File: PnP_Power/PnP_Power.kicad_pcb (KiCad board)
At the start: 2 copper layers, 25 parts, among them J1 S2B-PH-K-SLFSN, J2 S4B-PH-K-SLFSN, J3 S4B-PH-K-SLFSN, J4 S4B-PH-K-SLFSN, J5 S4B-PH-K-SLFSN, J6 S4B-PH-K-SLFSN, J7 S4B-PH-K-SLFSN

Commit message: Schematic and Layout Changes
updated schematic logic
added limit switches
added 12V to 5V dc converter
added power jack
added jumpers
added inverter for DIRSW

Started layout placed and organized everything nice. Should need to be adjusted some and then routed.
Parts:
- removed J2, J3, J4, J5, J6, J7: S4B-PH-K-SLFSN, PnP_Footprints:CONN_S4B-PH-K-S_JST
- removed R1: 1.5k, Resistor_SMD:R_0603_1608Metric_Pad0.98x0.95mm_HandSolder
- added C7: 22uF, Capacitor_SMD:C_0603_1608Metric_Pad1.08x0.95mm_HandSolder, F.Cu at (205.0, 145.8)
- added C8: 22uF, Capacitor_SMD:C_0603_1608Metric_Pad1.08x0.95mm_HandSolder, F.Cu at (200.5, 145.8)
- added C9: 0.1uF, Capacitor_SMD:C_0603_1608Metric_Pad1.08x0.95mm_HandSolder, F.Cu at (155.4, 75.2)
- added Conn1: Molex_SL_02, MRDT_Connectors:MOLEX_SL_02_Horizontal, F.Cu at (115.7, 143.3)
- added Conn10: Molex_SL_02, MRDT_Connectors:MOLEX_SL_02_Horizontal, F.Cu at (206.0, 153.5)
- added Conn11: Molex_SL_02, MRDT_Connectors:MOLEX_SL_02_Horizontal, F.Cu at (195.2, 153.5)
- added Conn12: Molex_SL_02, MRDT_Connectors:MOLEX_SL_02_Horizontal, F.Cu at (185.2, 153.5)
- added Conn13: Molex_SL_02, MRDT_Connectors:MOLEX_SL_02_Horizontal, F.Cu at (175.2, 153.5)
- added Conn14: Molex_SL_02, MRDT_Connectors:MOLEX_SL_02_Horizontal, F.Cu at (165.1, 153.5)
- added Conn15: Molex_SL_02, MRDT_Connectors:MOLEX_SL_02_Horizontal, F.Cu at (155.1, 153.5)
- added Conn2: Molex_SL_04, MRDT_Connectors:MOLEX_SL_04_Horizontal, F.Cu at (116.8, 66.0)
- added Conn3: Molex_SL_04, MRDT_Connectors:MOLEX_SL_04_Horizontal, F.Cu at (116.8, 119.1)
- added Conn4: Molex_SL_04, MRDT_Connectors:MOLEX_SL_04_Horizontal, F.Cu at (214.8, 121.4)
- added Conn5: Molex_SL_04, MRDT_Connectors:MOLEX_SL_04_Horizontal, F.Cu at (117.2, 92.2)
- added Conn6: Molex_SL_04, MRDT_Connectors:MOLEX_SL_04_Horizontal, F.Cu at (214.5, 95.0)
- added Conn7: Molex_SL_04, MRDT_Connectors:MOLEX_SL_04_Horizontal, F.Cu at (214.5, 68.3)
- added Conn8: Molex_SL_03, MRDT_Connectors:MOLEX_SL_03_Horizontal, F.Cu at (145.0, 153.5)
- added Conn9: Molex_SL_03, MRDT_Connectors:MOLEX_SL_03_Horizontal, F.Cu at (132.5, 153.5)
- added JP1: Jumper_2_Bridged, Connector_PinHeader_2.54mm:PinHeader_1x02_P2.54mm_Vertical, F.Cu at (131.8, 68.6)
- added JP10: Jumper_2_Bridged, Connector_PinHeader_2.54mm:PinHeader_1x02_P2.54mm_Vertical, F.Cu at (199.9, 66.0)
- added JP11: Jumper_2_Bridged, Connector_PinHeader_2.54mm:PinHeader_1x02_P2.54mm_Vertical, F.Cu at (199.9, 63.5)
- added JP12: Jumper_2_Bridged, Connector_PinHeader_2.54mm:PinHeader_1x02_P2.54mm_Vertical, F.Cu at (199.9, 61.0)
- added JP13: Jumper_2_Bridged, Connector_PinHeader_2.54mm:PinHeader_1x02_P2.54mm_Vertical, F.Cu at (199.6, 92.2)
- added JP14: Jumper_2_Bridged, Connector_PinHeader_2.54mm:PinHeader_1x02_P2.54mm_Vertical, F.Cu at (199.6, 89.6)
- added JP15: Jumper_2_Bridged, Connector_PinHeader_2.54mm:PinHeader_1x02_P2.54mm_Vertical, F.Cu at (199.6, 87.1)
- added JP16: Jumper_2_Bridged, Connector_PinHeader_2.54mm:PinHeader_1x02_P2.54mm_Vertical, F.Cu at (131.8, 95.0)
- added JP17: Jumper_2_Bridged, Connector_PinHeader_2.54mm:PinHeader_1x02_P2.54mm_Vertical, F.Cu at (131.8, 97.5)
- added JP18: Jumper_2_Bridged, Connector_PinHeader_2.54mm:PinHeader_1x02_P2.54mm_Vertical, F.Cu at (131.8, 100.1)
- added JP2: Jumper_2_Bridged, Connector_PinHeader_2.54mm:PinHeader_1x02_P2.54mm_Vertical, F.Cu at (131.8, 71.1)
- added JP3: Jumper_2_Bridged, Connector_PinHeader_2.54mm:PinHeader_1x02_P2.54mm_Vertical, F.Cu at (131.8, 73.7)
- added JP4: Jumper_2_Bridged, Connector_PinHeader_2.54mm:PinHeader_1x02_P2.54mm_Vertical, F.Cu at (131.8, 121.7)
- added JP5: Jumper_2_Bridged, Connector_PinHeader_2.54mm:PinHeader_1x02_P2.54mm_Vertical, F.Cu at (131.8, 124.2)
- added JP6: Jumper_2_Bridged, Connector_PinHeader_2.54mm:PinHeader_1x02_P2.54mm_Vertical, F.Cu at (131.8, 126.7)
- added JP7: Jumper_2_Bridged, Connector_PinHeader_2.54mm:PinHeader_1x02_P2.54mm_Vertical, F.Cu at (199.9, 118.9)
- added JP8: Jumper_2_Bridged, Connector_PinHeader_2.54mm:PinHeader_1x02_P2.54mm_Vertical, F.Cu at (199.9, 116.3)
- added JP9: Jumper_2_Bridged, Connector_PinHeader_2.54mm:PinHeader_1x02_P2.54mm_Vertical, F.Cu at (199.9, 113.8)
- added R6: 3.3k, Resistor_SMD:R_0603_1608Metric_Pad0.98x0.95mm_HandSolder, F.Cu at (155.4, 64.0)
- added R7: 3.3k, Resistor_SMD:R_0603_1608Metric_Pad0.98x0.95mm_HandSolder, F.Cu at (155.4, 68.0)
- added R8: 1k, Resistor_SMD:R_0603_1608Metric_Pad0.98x0.95mm_HandSolder, F.Cu at (155.4, 66.0)
- added U7: VNH5019A-E, Package_SO:ST_MultiPowerSO-30, F.Cu at (168.2, 67.1)
- added U8: LMS78_05-2.0R, PnP_Footprints:LMS78_05-2.0R, F.Cu at (202.6, 131.2)
- added U9: SN74LVC2G04DBVR, PnP_Footprints:SOT95P280X145-6N, F.Cu at (154.9, 71.1)
- C1, C2, C3, C4, C5, C6: footprint Capacitor_THT:CP_Radial_D8.0mm_P2.50mm -> Capacitor_THT:CP_Radial_D8.0mm_P3.50mm
- J1: value S2B-PH-K-SLFSN -> Barrel Jack 5mm x 2.5mm 54-00356; footprint PnP_Footprints:CONN_S2B-PH-K-S_JST -> PnP_Footprints:TENSILITY_54-00356
- moved D1 193.3 mm to (224.9, 149.9), turned to 180 degrees
- moved D2 182.7 mm to (215.4, 149.9), turned to 180 degrees
- moved R2 180.8 mm to (220.4, 149.8)
- moved J1 180.3 mm to (218.9, 142.7), turned to 90 degrees
- moved R3 171.1 mm to (211.0, 149.9)
- moved C5 153.8 mm to (215.9, 110.8), turned to -90 degrees
- moved U1 148.3 mm to (203.0, 134.5), turned to 180 degrees
- moved C2 118.0 mm to (215.4, 84.0), turned to -90 degrees
- moved C1 117.6 mm to (215.7, 57.8), turned to -90 degrees
- moved U6 94.5 mm to (203.0, 81.6), turned to 180 degrees
- moved U5 93.3 mm to (202.7, 107.8), turned to 180 degrees
- moved U3 75.6 mm to (128.7, 53.0)
- moved C4 75.5 mm to (115.8, 76.8)
- moved C6 56.4 mm to (115.8, 129.7)
- moved U2 55.8 mm to (128.7, 106.1)
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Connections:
- A1 pad 23: unconnected-(A1-Pad23) -> LS1
- A1 pad 24: unconnected-(A1-Pad24) -> EN3
- A1 pad 25: unconnected-(A1-Pad25) -> LS2
- A1 pad 26: unconnected-(A1-Pad26) -> STEP3
- A1 pad 27: unconnected-(A1-Pad27) -> LS3
- A1 pad 28: unconnected-(A1-Pad28) -> DIR3
- A1 pad 29: unconnected-(A1-Pad29) -> LS4
- A1 pad 30: unconnected-(A1-Pad30) -> EN2
- A1 pad 31: unconnected-(A1-Pad31) -> LS5
- A1 pad 33: unconnected-(A1-Pad33) -> LS6
- A1 pad 34: unconnected-(A1-Pad34) -> DIR2
- A1 pad 36: unconnected-(A1-Pad36) -> STEP2
- A1 pad 37: unconnected-(A1-Pad37) -> LED1
- A1 pad 38: unconnected-(A1-Pad38) -> EN6
- A1 pad 39: unconnected-(A1-Pad39) -> LED2
- A1 pad 3V3: unconnected-(A1-+3V3-Pad3V3) -> +3V3
- A1 pad 46: unconnected-(A1-Pad46) -> STEP4
- A1 pad 48: unconnected-(A1-Pad48) -> DIR4
- A1 pad 49: unconnected-(A1-Pad49) -> STEP1
- A1 pad 5: unconnected-(A1-Pad5) -> VACDIR
- A1 pad 51: unconnected-(A1-Pad51) -> DIR1
- A1 pad 53: unconnected-(A1-Pad53) -> EN1
- A1 pad 5V_1: unconnected-(A1-+5V_1-Pad5V_1) -> +5V
- A1 pad 5V_2: unconnected-(A1-+5V_2-Pad5V_2) -> +5V
- A1 pad 5V_3: unconnected-(A1-+5V_3-Pad5V_3) -> +5V
- A1 pad 8: unconnected-(A1-Pad8) -> PWM
- A1 pad AD0: unconnected-(A1-PadAD0) -> STEP6
- A1 pad AD1: unconnected-(A1-PadAD1) -> DIR6
- A1 pad AD2: unconnected-(A1-PadAD2) -> EN5
- A1 pad AD6: unconnected-(A1-PadAD6) -> STEP5
- A1 pad AD7: unconnected-(A1-PadAD7) -> DIR5
- A1 pad AD8: unconnected-(A1-PadAD8) -> EN4
- A1 pad GND1: unconnected-(A1-PadGND1) -> GND
- A1 pad GND2: unconnected-(A1-PadGND2) -> GND
- A1 pad GND3: unconnected-(A1-PadGND3) -> GND
- A1 pad GND4: unconnected-(A1-PadGND4) -> GND
- A1 pad GND5: unconnected-(A1-PadGND5) -> GND
- U1 pad 11: SLP1 -> +5V
- U1 pad 12: RES1 -> +5V
- U1 pad 13: MS3_1 -> Net-(JP7-A)
- U1 pad 14: MS2_1 -> Net-(JP8-A)
- U1 pad 15: MS1_1 -> Net-(JP9-A)
- U2 pad 11: SLP2 -> +5V
- U2 pad 12: RES2 -> +5V
- U2 pad 13: MS3_2 -> Net-(JP4-A)
- U2 pad 14: MS2_2 -> Net-(JP5-A)
- U2 pad 15: MS1_2 -> Net-(JP6-A)
- U3 pad 11: SLP3 -> +5V
- U3 pad 12: RES3 -> +5V
- U3 pad 13: MS3_3 -> Net-(JP1-A)
- U3 pad 14: MS2_3 -> Net-(JP2-A)
- U3 pad 15: MS1_3 -> Net-(JP3-A)
- U4 pad 11: SLP4 -> +5V
- U4 pad 12: RES4 -> +5V
- U4 pad 13: MS3_4 -> Net-(JP16-A)
- U4 pad 14: MS2_4 -> Net-(JP17-A)
- U4 pad 15: MS1_4 -> Net-(JP18-A)
- U5 pad 11: SLP5 -> +5V
- U5 pad 12: RES5 -> +5V
- U5 pad 13: MS3_5 -> Net-(JP13-A)
- U5 pad 14: MS2_5 -> Net-(JP14-A)
- U5 pad 15: MS1_5 -> Net-(JP15-A)
- U6 pad 11: SLP6 -> +5V
- U6 pad 12: RES6 -> +5V
- U6 pad 13: MS3_6 -> Net-(JP10-A)
- U6 pad 14: MS2_6 -> Net-(JP11-A)
- U6 pad 15: MS1_6 -> Net-(JP12-A)
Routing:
- net Net-(JP15-A): track 0.00 -> 3.31 mm
- net Net-(JP14-A): track 0.00 -> 3.31 mm
- net Net-(JP13-A): track 0.00 -> 3.31 mm
- net Net-(JP18-A): track 0.00 -> 3.31 mm
- net Net-(JP17-A): track 0.00 -> 3.31 mm
- net Net-(JP16-A): track 0.00 -> 3.31 mm
- net Net-(JP12-A): track 0.00 -> 3.31 mm
- net Net-(JP11-A): track 0.00 -> 3.31 mm
- net Net-(JP10-A): track 0.00 -> 3.31 mm
- net Net-(JP9-A): track 0.00 -> 3.30 mm
- net Net-(JP8-A): track 0.00 -> 3.30 mm
- net Net-(JP7-A): track 0.00 -> 3.30 mm
- net Net-(JP6-A): track 0.00 -> 3.30 mm
- net Net-(JP5-A): track 0.00 -> 3.30 mm
- net Net-(JP4-A): track 0.00 -> 3.30 mm
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- added copper zone on B.Cu, net GND
- added copper zone on F.Cu, net GND

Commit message: Idek
layouts and stuff and 3d model
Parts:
- added H1: MountingHole, MountingHole:MountingHole_2.2mm_M2, F.Cu at (107.7, 52.3)
- added H2: MountingHole, MountingHole:MountingHole_2.2mm_M2, F.Cu at (223.3, 52.3)
- added H3: MountingHole, MountingHole:MountingHole_2.2mm_M2, F.Cu at (107.7, 158.5)
- added H4: MountingHole, MountingHole:MountingHole_2.2mm_M2, F.Cu at (223.3, 158.5)
- moved D1 82.3 mm to (222.2, 67.6)
- moved D2 82.3 mm to (214.0, 67.6)
- moved R3 82.3 mm to (209.6, 67.6)
- moved R2 82.3 mm to (218.3, 67.6)
- moved J1 81.8 mm to (218.6, 60.9)
- moved Conn1 81.5 mm to (117.2, 61.7)
- moved C8 76.9 mm to (198.5, 68.9)
- moved U8 76.9 mm to (200.7, 54.3)
- moved C7 76.9 mm to (203.2, 68.9)
- moved C2 13.7 mm to (215.4, 97.8)
- moved C5 13.7 mm to (215.9, 124.5)
- moved Conn4 13.7 mm to (214.8, 135.2)
- moved Conn6 13.7 mm to (214.5, 108.7)
- moved Conn7 13.7 mm to (214.5, 82.0)
- moved JP13 13.7 mm to (199.6, 105.9)
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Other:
- board outline added: 120.7 x 111.3 mm

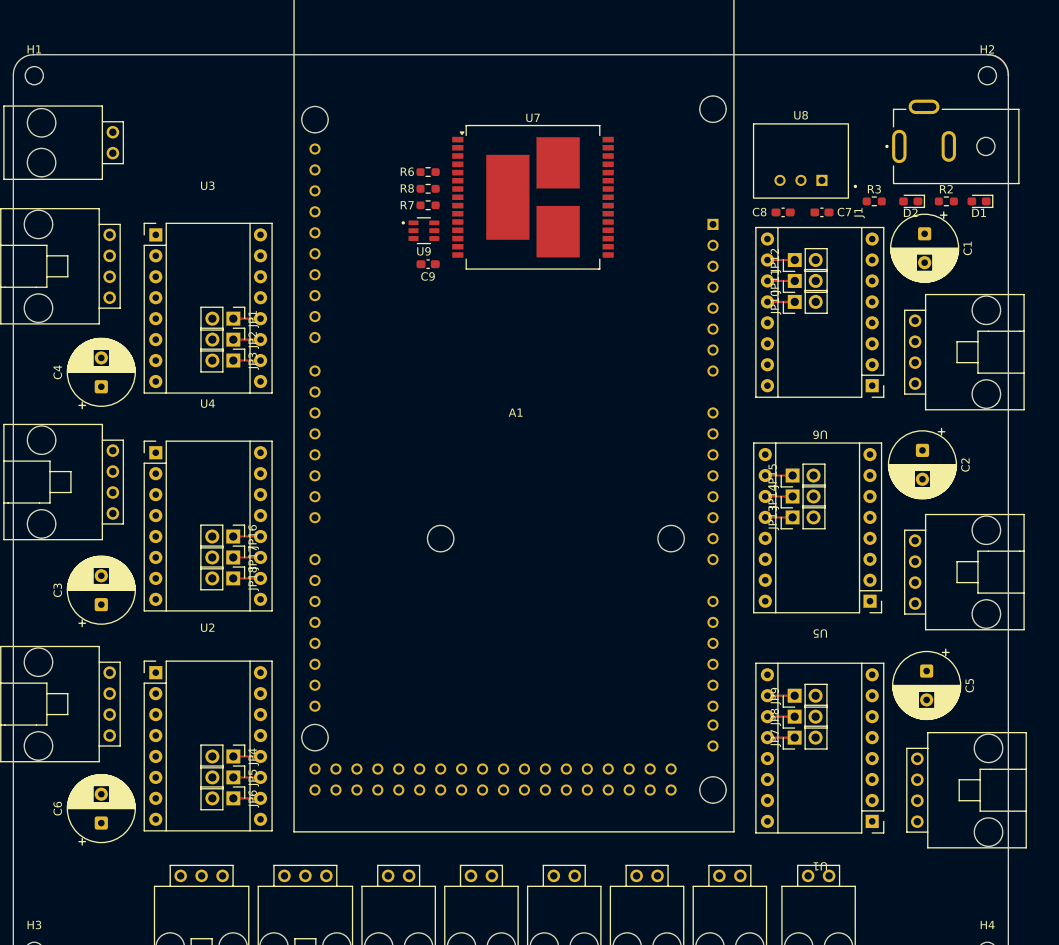
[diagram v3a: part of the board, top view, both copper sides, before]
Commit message: Routed and Labeled layout
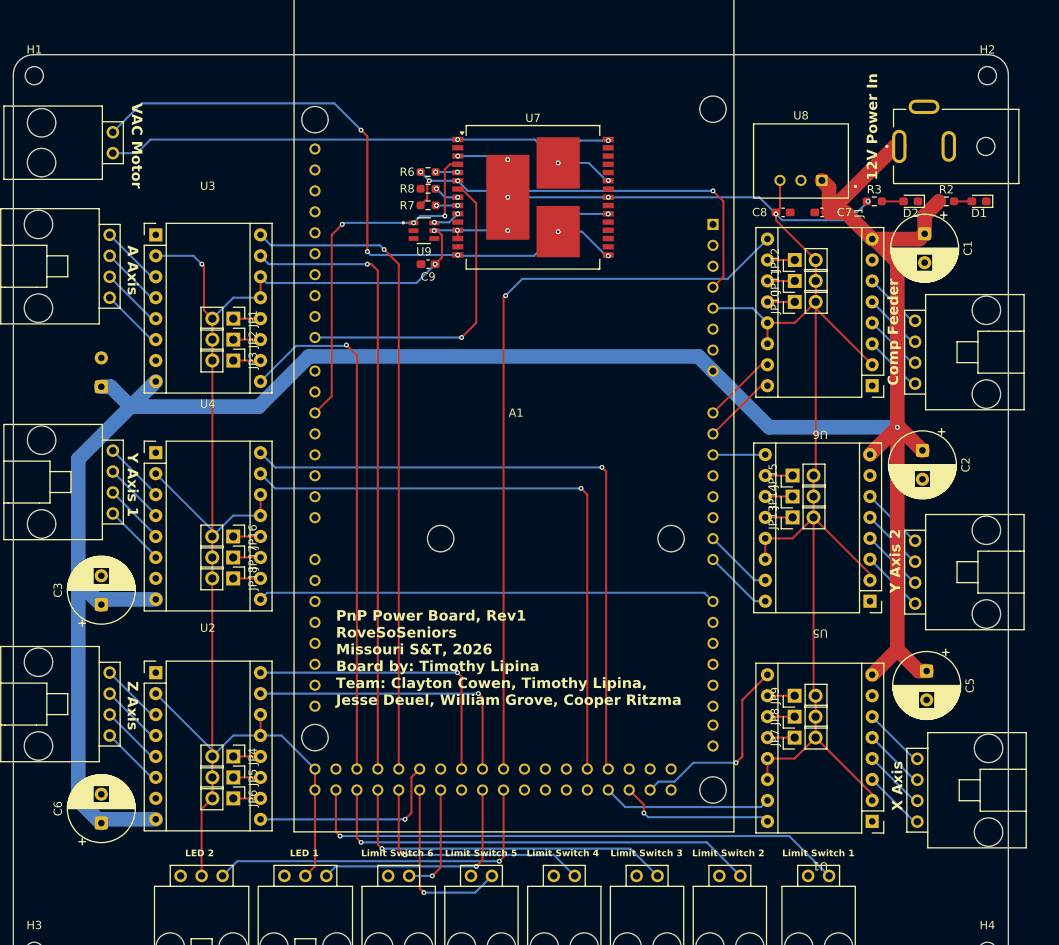
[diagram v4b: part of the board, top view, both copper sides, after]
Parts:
- C4: moved to B.Cu
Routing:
- net +5V: track 0.00 -> 379.3 mm, vias 0 -> 11
- net +12V: track 0.00 -> 289.1 mm, vias 0 -> 1
- net EN6: track 0.00 -> 92.1 mm, vias 0 -> 1
- net /OUTB: track 0.00 -> 86.9 mm, vias 0 -> 6
- net DIR3: track 0.00 -> 79.5 mm, vias 0 -> 1
- net DIR4: track 0.00 -> 79.0 mm, vias 0 -> 1
- net STEP3: track 0.00 -> 75.4 mm, vias 0 -> 1
- net STEP4: track 0.00 -> 74.0 mm, vias 0 -> 1
- net /OUTA: track 0.00 -> 70.2 mm, vias 0 -> 4
- net LS1: track 0.00 -> 67.1 mm, vias 0 -> 1
- net EN3: track 0.00 -> 64.2 mm, vias 0 -> 1
- net EN4: track 0.00 -> 55.6 mm
- net LS2: track 0.00 -> 54.2 mm, vias 0 -> 1
- net +3V3: track 0.00 -> 52.6 mm, vias 0 -> 4
- net VACDIR: track 0.00 -> 44.6 mm, vias 0 -> 3
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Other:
- board text added: "12V Power In"
- board text added: "A Axis"
- board text added: "Comp Feeder"
- board text added: "LED 1"
- board text added: "LED 2"
- board text added: "Limit Switch 1"
- board text added: "Limit Switch 2"
- board text added: "Limit Switch 3"
- board text added: "Limit Switch 4"
- board text added: "Limit Switch 5"
- board text added: "Limit Switch 6"
- board text added: "PnP Power Board, Rev1 RoveSoSeniors Missouri S&T, 2026 Board by: Timothy Lipina Team: Clayton Cowen, Timothy Lipina, Jesse Deuel, William Grove, Cooper Ritzma"
- board text added: "VAC Motor"
- board text added: "X Axis"
- board text added: "Y Axis 1"
- board text added: "Y Axis 2"
- board text added: "Z Axis"
